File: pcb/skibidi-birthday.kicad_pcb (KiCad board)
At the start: 2 copper layers, 90 x 50 mm, 34 parts, among them J1 USB_C_Receptacle_USB2.0_16P, J2 USB_C_Receptacle_USB2.0_16P, J3 USB_C_Receptacle_USB2.0_16P, J4 USB_C_Receptacle_USB2.0_16P, J5 USB_C_Receptacle_USB2.0_16P, U1 USBLC6-2SC6, U2 CH334P, U3 USBLC6-2SC6, U4 USBLC6-2SC6, U5 USBLC6-2SC6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

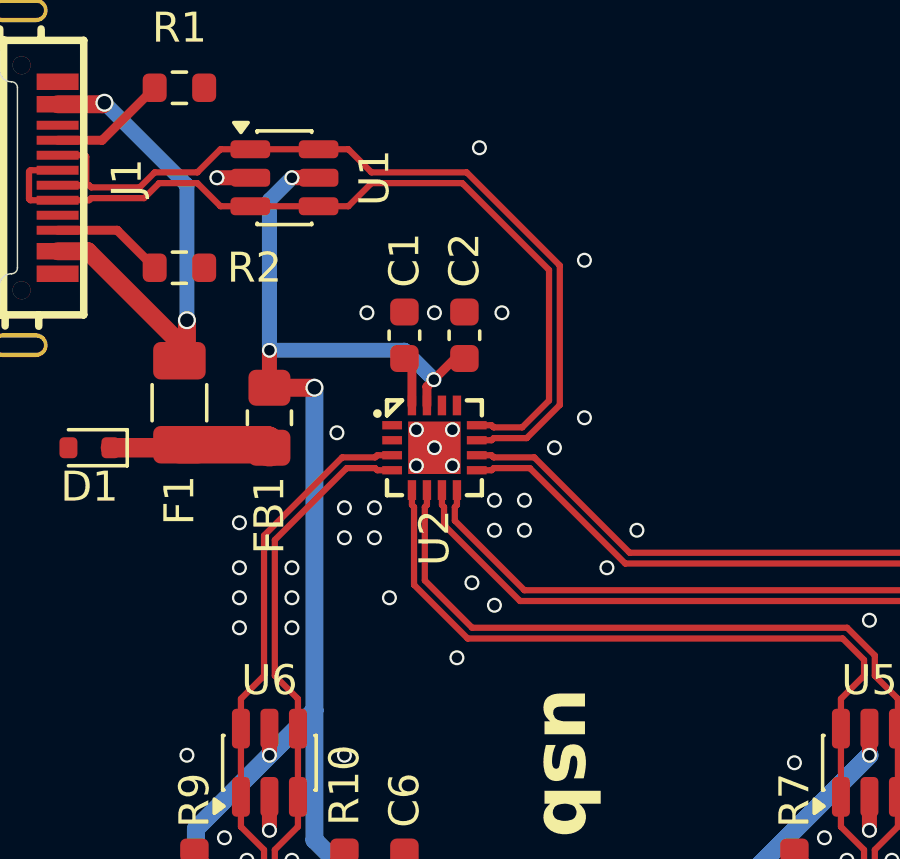
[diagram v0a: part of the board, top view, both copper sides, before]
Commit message: forgot to length match for the 67th time
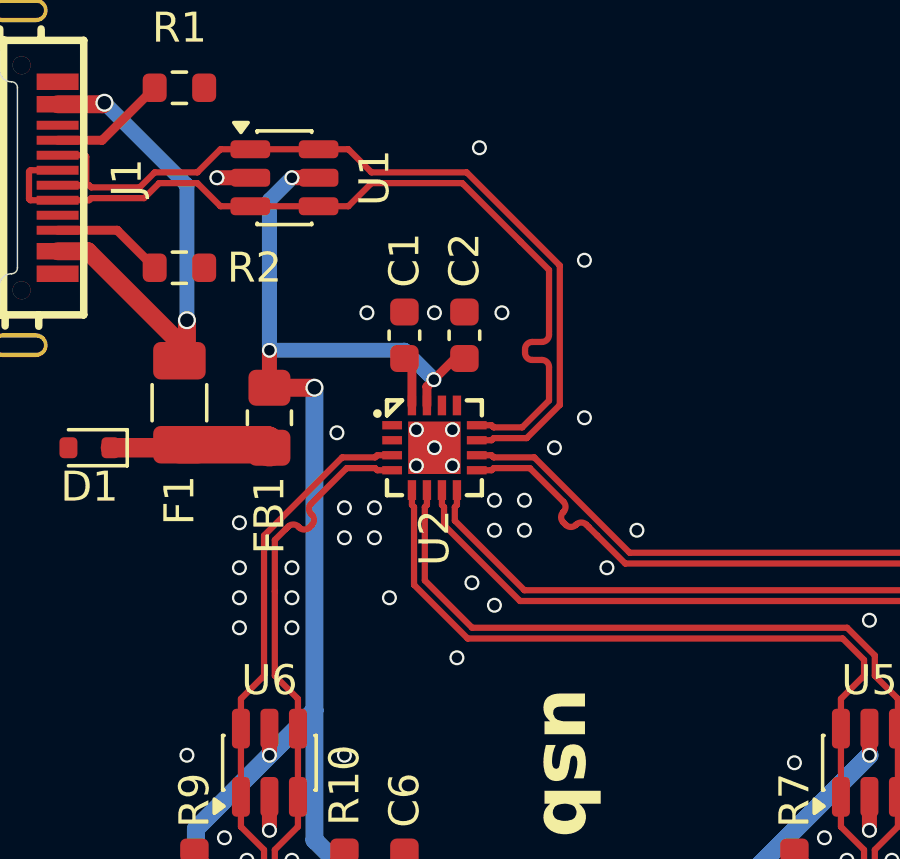
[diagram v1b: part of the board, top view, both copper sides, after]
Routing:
- net /UD+: track 28.5 -> 29.6 mm
- net /4D+: track 23.6 -> 24.2 mm
- net /1D-: track 70.5 -> 71.0 mm
